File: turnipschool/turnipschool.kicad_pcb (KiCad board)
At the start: 4 copper layers, 22.5 x 12 mm, 62 parts, among them J1 USB-DEVICE-SHIELD, P1 CONN_1, P2 RESET_N, P3 DD, P4 DC, P5 3V3, P6 GND, P7 CABLE, T1 BALUN, U1 CC1111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

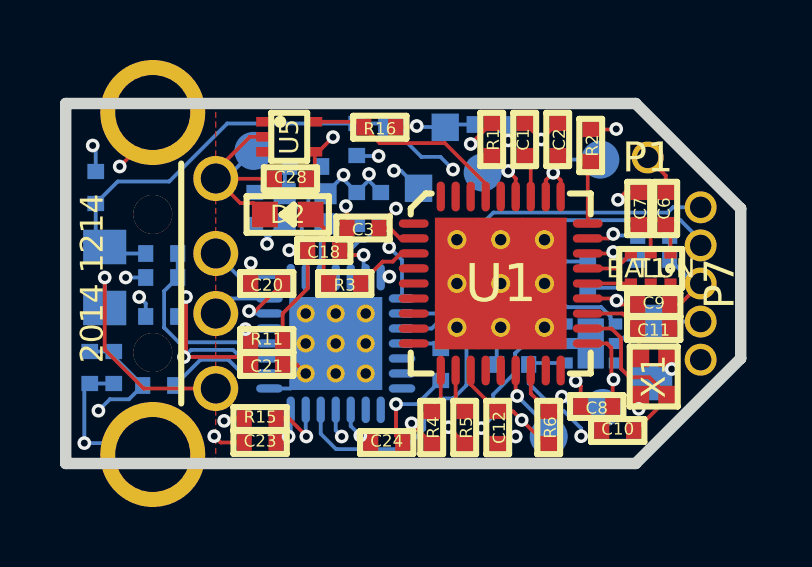
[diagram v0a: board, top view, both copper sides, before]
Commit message: corrected hub supply connections, added required 1.5k USB pull-up, removed debug LED
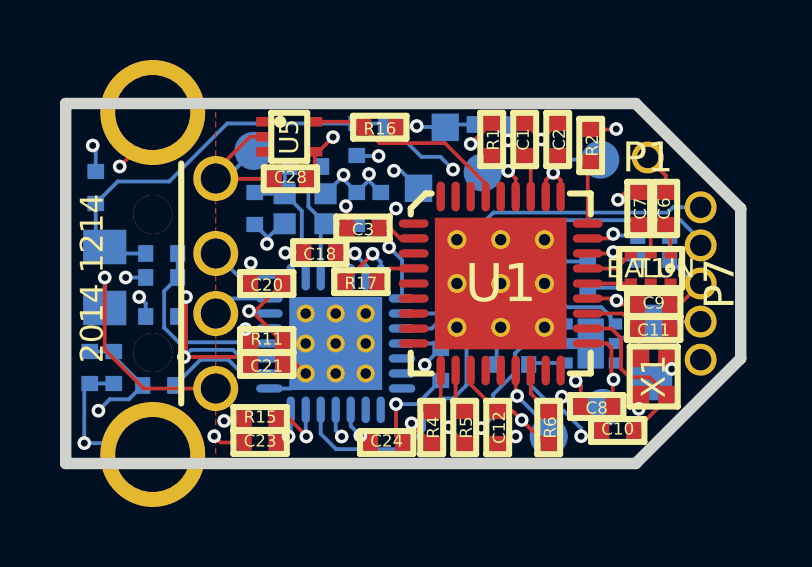
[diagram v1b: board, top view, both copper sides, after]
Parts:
- removed D2: LED1, cc1111-legacy:GSG-0603D
- removed R3: 330, cc1111-legacy:GSG-0402
- added R17: 1.5k, cc1111-legacy:GSG-0402, F.Cu at (99.8, 89.9)
- moved C18 0.15 mm to (98.5, 89.0)
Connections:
- C18 pad 1: 3V3 -> GND
- C18 pad 2: Net-(C18-Pad2) -> 3V3
- C20 pad 1: 3V3 -> GND
- C20 pad 2: Net-(C20-Pad2) -> 3V3
- C22 pad 1: Net-(C22-Pad1) -> 3V3
- C22 pad 2: 3V3 -> GND
- C23 pad 1: Net-(C23-Pad1) -> 3V3
- C23 pad 2: 3V3 -> GND
- C24 pad 1: 3V3 -> GND
- C24 pad 2: Net-(C24-Pad2) -> 3V3
- U1 pad 1: Net-(U1-Pad1) -> (no net)
- U1 pad 13: Net-(U1-Pad13) -> (no net)
- U1 pad 14: Net-(U1-Pad14) -> (no net)
- U1 pad 17: Net-(U1-Pad17) -> (no net)
- U1 pad 18: Net-(U1-Pad18) -> (no net)
- U1 pad 3: Net-(R3-Pad2) -> (no net)
- U1 pad 32: Net-(U1-Pad32) -> (no net)
- U1 pad 34: Net-(U1-Pad34) -> (no net)
- U1 pad 35: Net-(U1-Pad35) -> (no net)
- U1 pad 36: Net-(U1-Pad36) -> (no net)
- U1 pad 5: Net-(U1-Pad5) -> (no net)
- U1 pad 6: Net-(U1-Pad6) -> (no net)
- U1 pad 7: Net-(U1-Pad7) -> (no net)
- U1 pad 8: Net-(U1-Pad8) -> (no net)
- U1 pad 9: Net-(U1-Pad9) -> (no net)
- U3 pad 10: Net-(C24-Pad2) -> 3V3
- U3 pad 14: Net-(C23-Pad1) -> 3V3
- U3 pad 20: Net-(C20-Pad2) -> 3V3
- U3 pad 25: Net-(U3-Pad25) -> (no net)
- U3 pad 27: Net-(C18-Pad2) -> 3V3
- U3 pad 4: Net-(C22-Pad1) -> 3V3
- U3 pad 5: Net-(U3-Pad5) -> (no net)
- U3 pad 6: Net-(U3-Pad6) -> (no net)
- U3 pad 7: Net-(U3-Pad7) -> (no net)
- U3 pad 8: Net-(U3-Pad8) -> (no net)
- U3 pad 9: Net-(U3-Pad9) -> (no net)
- U4 pad 6: Net-(U4-Pad6) -> (no net)
- U5 pad 1: Net-(U5-Pad1) -> (no net)
- U5 pad 3: Net-(U5-Pad3) -> (no net)
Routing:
- net GND: track 43.3 -> 46.7 mm, vias 18 -> 22
- net Net-(D2-Pad1): track 2.60 -> 0.00 mm
- net Net-(R3-Pad2): track 2.57 -> 0.00 mm
- net Net-(C20-Pad2): track 2.22 -> 0.00 mm, vias 1 -> 0
- net 3V3: track 33.7 -> 35.7 mm, vias 15 -> 16
- net Net-(R17-Pad2): track 0.00 -> 1.70 mm
- net Net-(C18-Pad2): track 1.63 -> 0.00 mm, vias 1 -> 0
- net Net-(C24-Pad2): track 1.43 -> 0.00 mm, vias 1 -> 0
- net Net-(C23-Pad1): track 1.42 -> 0.00 mm, vias 1 -> 0
- net Net-(C22-Pad1): track 1.36 -> 0.00 mm
- net Net-(R17-Pad1): track 10.9 -> 12.0 mm
- net Net-(R9-Pad1): track 2.29 -> 2.85 mm

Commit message: swapped downstream USB ports, made CC1111 port removable on the hub, improved layout
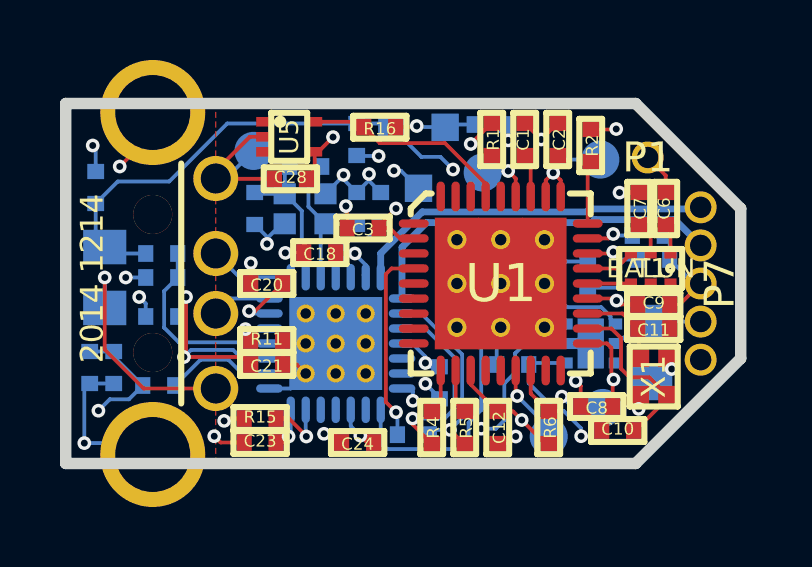
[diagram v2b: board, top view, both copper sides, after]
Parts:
- R17: moved to B.Cu
- moved R17 5.39 mm to (101.6, 95.0), turned to 180 degrees
- moved C24 0.97 mm to (99.7, 95.3), turned to 0 degrees
- moved C22 0.61 mm to (102.5, 93.3)
- moved C5 0.18 mm to (109.4, 88.4)
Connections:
- R11 pad 1: 3V3 -> GND
- U3 pad 1: Net-(R4-Pad1) -> /USBDP_DN2
- U3 pad 11: Net-(U3-Pad11) -> (no net)
- U3 pad 12: Net-(U3-Pad12) -> (no net)
- U3 pad 2: /USBDM_DN2 -> Net-(R17-Pad1)
- U3 pad 28: Net-(R17-Pad1) -> /USBDM_DN2
- U3 pad 3: /USBDP_DN2 -> Net-(R4-Pad1)
- U3 pad 7: (no net) -> Net-(U3-Pad7)
- U3 pad 8: (no net) -> Net-(U3-Pad8)
- U4 pad 3: Net-(U3-Pad11) -> Net-(U3-Pad7)
- U4 pad 4: Net-(U3-Pad12) -> Net-(U3-Pad8)
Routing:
- net Net-(U3-Pad12): track 14.5 -> 0.00 mm
- net Net-(U3-Pad8): track 0.00 -> 13.5 mm
- net Net-(U3-Pad11): track 11.8 -> 0.00 mm, vias 2 -> 0
- net Net-(U3-Pad7): track 0.00 -> 9.49 mm, vias 0 -> 2
- net Net-(R17-Pad1): track 12.0 -> 6.88 mm, vias 2 -> 1
- net Net-(R17-Pad2): track 1.70 -> 6.60 mm, vias 0 -> 1
- net Net-(R4-Pad1): track 10.8 -> 6.64 mm, vias 2 -> 1
- net 3V3: track 35.7 -> 34.7 mm
- net /USBDM_DN2: track 12.8 -> 12.0 mm
- net GND: track 46.7 -> 46.0 mm, vias 22 -> 23
- net /USBDP_DN2: track 13.3 -> 12.6 mm

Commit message: improved supply zones
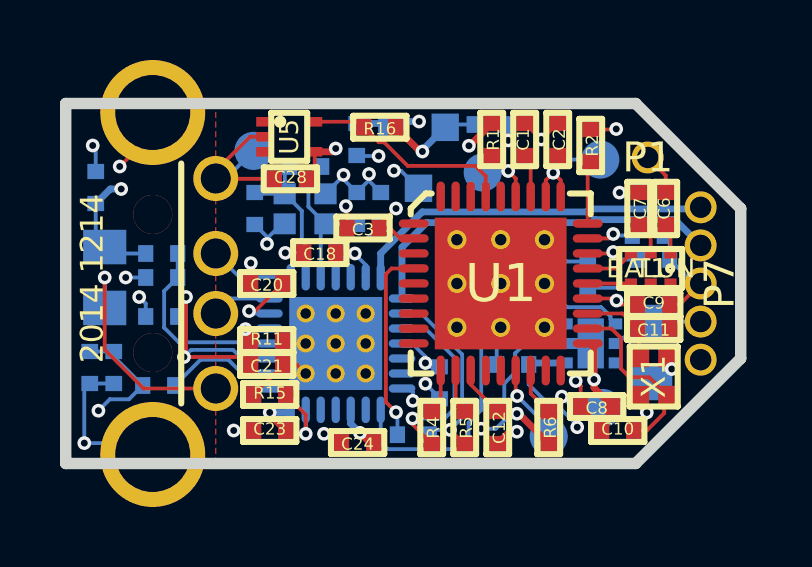
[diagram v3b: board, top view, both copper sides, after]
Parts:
- moved R15 0.86 mm to (96.8, 93.7)
- moved C23 0.51 mm to (96.8, 94.9)
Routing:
- net /VBUS: track 31.8 -> 10.4 mm, vias 2 -> 3
- net 3V3: track 34.7 -> 39.4 mm
- net GND: track 46.0 -> 46.7 mm, vias 23 -> 22
- net Net-(R16-Pad1): track 6.99 -> 7.59 mm
- added copper zone on C3, net /SHIELD
- added copper zone on C3, net /VBUS

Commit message: general layout cleanup
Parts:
- C22: moved to F.Cu
- moved C22 1.74 mm to (100.7, 93.1)
- moved P2 0.84 mm to (104.7, 86.2)
- moved P3 0.07 mm to (106.0, 95.1)
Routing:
- net Net-(R17-Pad2): track 6.60 -> 8.19 mm
- net Net-(C26-Pad1): track 6.04 -> 7.46 mm
- net GND: track 46.7 -> 48.1 mm, vias 22 -> 17
- net Net-(R4-Pad1): track 6.64 -> 5.70 mm
- net /SHIELD: track 27.5 -> 26.7 mm
- net /RESET_N: track 2.59 -> 1.94 mm
